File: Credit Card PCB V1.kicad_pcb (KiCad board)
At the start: 2 copper layers, 85.5 x 54 mm, 49 parts, among them J1 USB_C_Receptacle_USB2.0, SW1 RotaryEncoder, U1 USBLC6-2SC6, U2 ATmega32U2-A, Y1 16MHz

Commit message: Large Update
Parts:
- removed REF** (x4): MountingHole_2.2mm_M2_DIN965_Pad, MountingHole:MountingHole_2.2mm_M2_DIN965_Pad
- added C2: 1uF, Capacitor_SMD:C_0603_1608Metric, B.Cu at (159.8, 69.8)
- added C3: 10uF, Capacitor_SMD:C_0603_1608Metric, B.Cu at (159.8, 71.2)
- added F1: PTC 500mA, Fuse:Fuse_0603_1608Metric, B.Cu at (156.2, 73.8)
- added H0: MountingHole_Pad, MountingHole:MountingHole_2.2mm_M2_Pad_Via, F.Cu at (87.8, 68.5)
- added H1: MountingHole_Pad, MountingHole:MountingHole_2.2mm_M2_Pad_Via, F.Cu at (166.2, 68.5)
- added H2: MountingHole_Pad, MountingHole:MountingHole_2.2mm_M2_Pad_Via, F.Cu at (87.8, 115.5)
- added H3: MountingHole_Pad, MountingHole:MountingHole_2.2mm_M2_Pad_Via, F.Cu at (166.2, 115.5)
- added SW0: SW_Push, Button_Switch_SMD:SW_SPST_EVQP7C, B.Cu at (145.0, 66.5)
- moved R9 79.9 mm to (87.8, 86.8), turned to 90 degrees
- moved R7 79.1 mm to (87.8, 106.8), turned to 90 degrees
- moved R8 78.5 mm to (87.8, 96.8), turned to -90 degrees
- moved R4 17.2 mm to (157.2, 70.5), turned to 90 degrees
- moved U1 15.4 mm to (152.8, 74.0), turned to 135 degrees
- moved R3 14.5 mm to (156.5, 76.2), turned to -45 degrees
- moved R5 13.4 mm to (126.0, 75.0), turned to 90 degrees
- moved R2 13.2 mm to (155.0, 77.8), turned to -45 degrees
- moved R6 11.7 mm to (128.0, 75.0), turned to 90 degrees
- moved R1 8.00 mm to (167.0, 91.2), turned to 90 degrees
- moved C1 5.53 mm to (151.2, 78.2)
- moved C10 2.46 mm to (160.5, 74.2), turned to 135 degrees
- moved C8 1.60 mm to (159.2, 75.5), turned to 135 degrees
- moved C6 0.75 mm to (166.5, 76.8)
- moved C7 0.56 mm to (162.2, 72.5)
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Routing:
- net Net-(D12-A): track 104.4 -> 2.99 mm
- net /Indicator 2: track 21.6 -> 121.3 mm
- net Net-(D13-A): track 99.7 -> 2.99 mm
- net /Indicator 1: track 18.9 -> 113.1 mm
- net Net-(D14-A): track 95.0 -> 2.99 mm
- net /Indicator 0: track 16.2 -> 104.9 mm
- net Net-(U2-PC1/~{RESET}): track 0.00 -> 46.2 mm
- net /V Bus: track 0.00 -> 41.5 mm, vias 0 -> 4
- net /D+ Bus: track 0.00 -> 32.6 mm, vias 0 -> 2
- net /D- Bus: track 0.00 -> 31.9 mm, vias 0 -> 2
- net +5V: track 11.8 -> 41.4 mm
- net Net-(U2-D+): track 19.3 -> 6.10 mm, vias 2 -> 0
- net Net-(U2-~{HWB}/PD7): track 11.6 -> 2.77 mm
- net Net-(U2-D-): track 14.5 -> 6.19 mm
- net GND: track 11.4 -> 4.69 mm, vias 0 -> 3
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
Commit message: Chunky Update
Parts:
- moved C9 0.75 mm to (167.0, 79.5)
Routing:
- net +5V: track 41.4 -> 40.6 mm
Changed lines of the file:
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@@
   )
   (setup
+    (stackup
+      (layer "F.SilkS" (type "Top Silk Screen"))
+      (layer "F.Paste" (type "Top Solder Paste"))
+      (layer "F.Mask" (type "Top Solder Mask") (thickness 0.01))
+      (layer "F.Cu" (type "copper") (thickness 0.035))
+      (layer "dielectric 1" (type "core") (thickness 1.51) (material "FR4") (epsilon_r 4.5) (loss_tangent 0.02))
+      (layer "B.Cu" (type "copper") (thickness 0.035))
+      (layer "B.Mask" (type "Bottom Solder Mask") (thickness 0.01))
+      (layer "B.Paste" (type "Bottom Solder Paste"))
+      (layer "B.SilkS" (type "Bottom Silk Screen"))
+      (copper_finish "None")
+      (dielectric_constraints no)
+    )
     (pad_to_mask_clearance 0)
     (aux_axis_origin 84.25 119)
@@
   )
   (footprint "Capacitor_SMD:C_0603_1608Metric" (layer "B.Cu")
-    (at 167.75 79.5 90)
+    (at 167 79.5 90)
     (descr "Capacitor SMD 0603 (1608 Metric), square (rectangular) end terminal, IPC_7351 nominal, (Body size source: IPC-SM-782 page 76, https://www.pcb-3d.com/wordpress/wp-content/uploads/ipc-sm-782a_amendment_1_and_2.pdf), generated with kicad-footprint-generator")
     (tags "capacitor")
@@
   (segment (start 162.809835 82.231408) (end 164.952906 82.231408) (width 0.25) (layer "B.Cu") (net 7))
   (segment (start 164.952906 82.231408) (end 165.472361 81.711953) (width 0.25) (layer "B.Cu") (net 7))
-  (segment (start 167.75 80.275) (end 166.909314 80.275) (width 0.25) (layer "B.Cu") (net 7))
   (segment (start 160.5 76.75) (end 160.5 79.921573) (width 0.25) (layer "B.Cu") (net 7))
   (segment (start 166.909314 80.275) (end 165.472361 81.711953) (width 0.25) (layer "B.Cu") (net 7))

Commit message: Another Chunky Update
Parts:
- F1: footprint Fuse:Fuse_0603_1608Metric -> Fuse:Fuse_1206_3216Metric
- R5, R6: value R_Small -> 5.1k
- SW0: footprint Button_Switch_SMD:SW_SPST_EVQP7C -> Button_Switch_SMD:SW_SPST_SKQG_WithStem
- moved C10 23.2 mm to (167.0, 96.5), turned to -135 degrees
- moved R4 10.8 mm to (146.8, 68.0), turned to 180 degrees
- moved C9 9.44 mm to (161.3, 72.0), turned to 0 degrees
- moved SW0 6.73 mm to (139.2, 70.0)
- moved C2 5.47 mm to (161.3, 75.0)
- moved C8 5.15 mm to (164.2, 74.2), turned to -90 degrees
- moved C7 4.74 mm to (166.9, 73.4), turned to 180 degrees
- moved Y1 3.06 mm to (166.9, 76.4), turned to -90 degrees
- moved C3 2.72 mm to (161.3, 73.5)
- moved C6 2.68 mm to (166.9, 79.4), turned to 0 degrees
- moved F1 2.29 mm to (158.5, 73.5), turned to -90 degrees
- moved R5 0.25 mm to (125.8, 75.0)
- moved R6 0.25 mm to (128.2, 75.0)
- moved R1 0.25 mm to (166.8, 91.1)
- moved J1 0.22 mm to (127.0, 68.7)
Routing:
- net +5V: track 40.6 -> 56.6 mm
- net Net-(U2-PC1/~{RESET}): track 46.2 -> 37.5 mm
- net /V Bus: track 41.5 -> 44.0 mm
- net Net-(U2-PC0/XTAL2): track 5.90 -> 4.20 mm
- net Net-(U2-XTAL1): track 10.8 -> 9.70 mm
- net /D+ Bus: track 32.6 -> 31.6 mm
- added copper zone on B.Cu, net +5V

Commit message: STUFF
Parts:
- moved D7 0.50 mm to (111.2, 104.5)
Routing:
- net Net-(D7-A): track 3.49 -> 2.99 mm
- net /Row 2: track 73.5 -> 74.0 mm

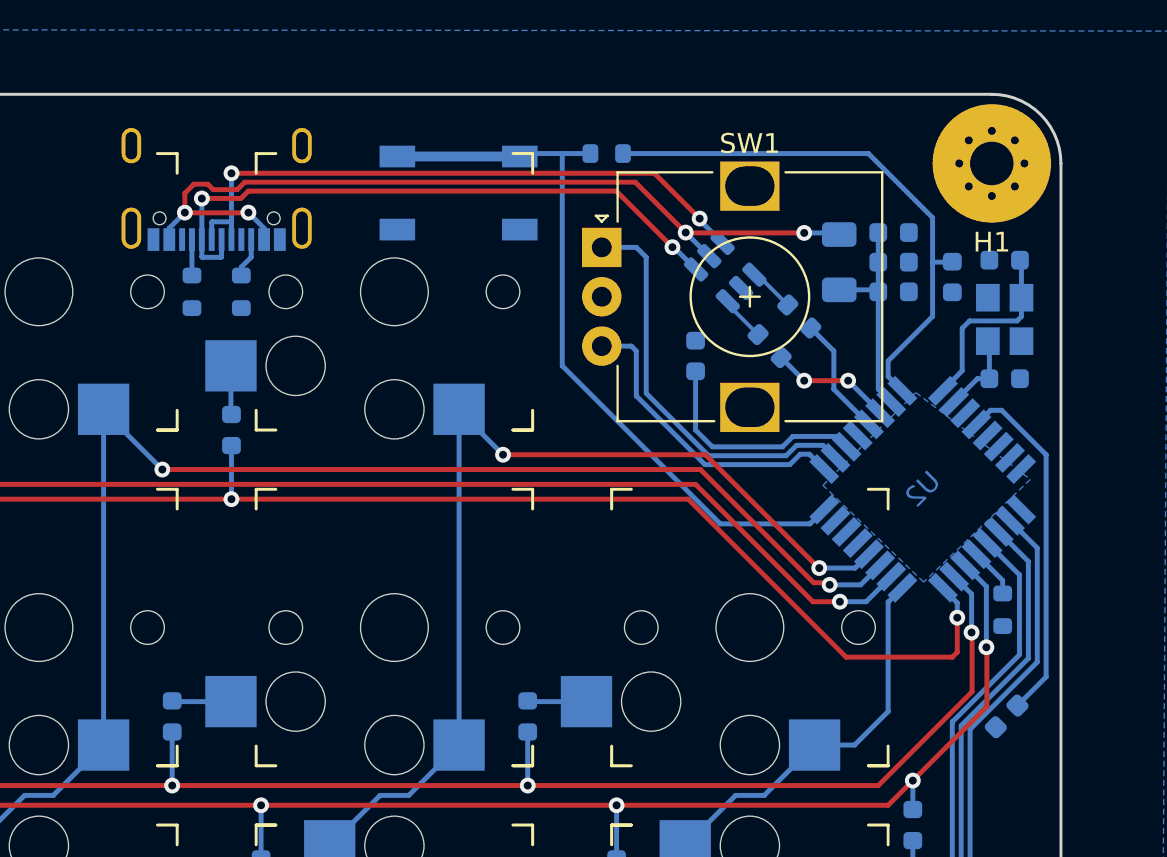
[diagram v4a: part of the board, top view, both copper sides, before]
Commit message: USB C Receptacle Change
Changed the usb c receptacle to a japanese standard one. I'm too lazy to go back and look up what it is.
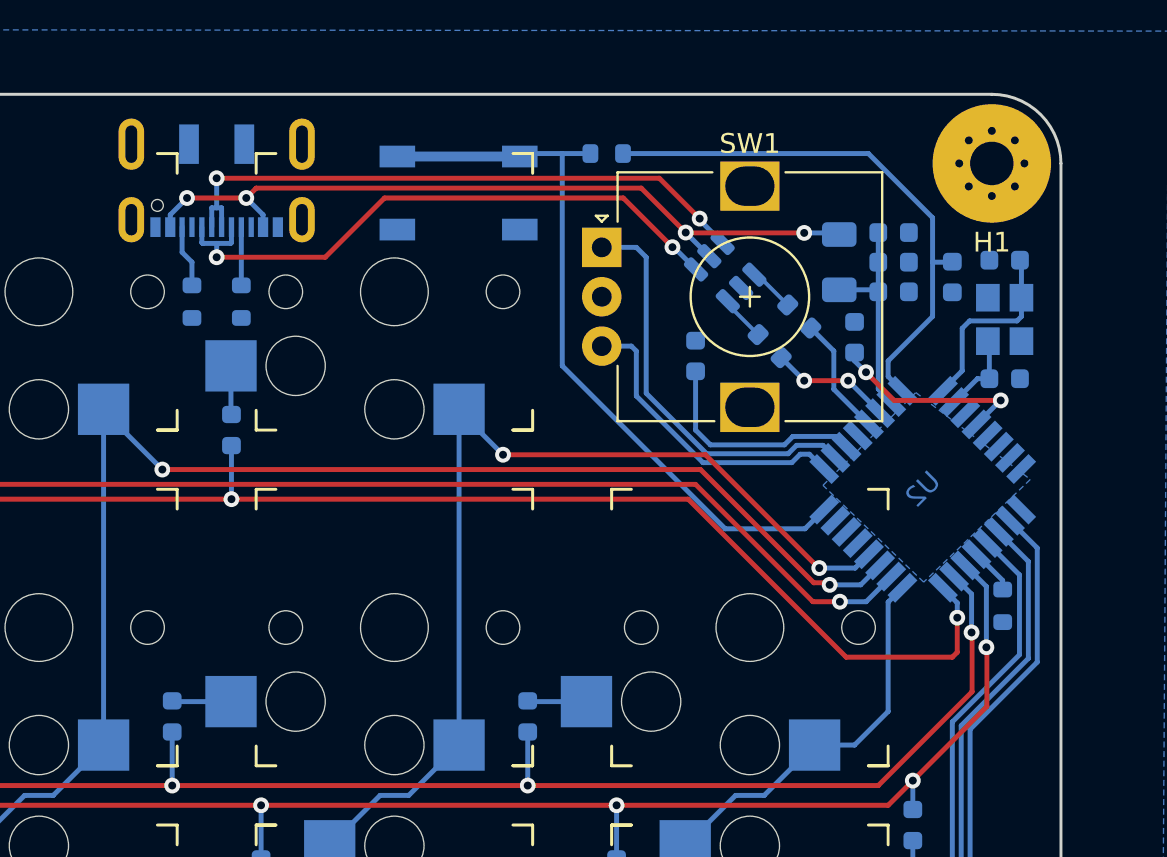
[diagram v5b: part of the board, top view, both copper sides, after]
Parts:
- J1: footprint Connector_USB:USB_C_Receptacle_GCT_USB4105-xx-A_16P_TopMnt_Horizontal -> Connector_USB:USB_C_Receptacle_JAE_DX07S016JA1R1500
- moved C10 20.7 mm to (159.3, 77.3), turned to 90 degrees
- moved R5 0.50 mm to (125.8, 75.5)
- moved R6 0.50 mm to (128.2, 75.5)
- moved R1 0.20 mm to (166.8, 90.9)
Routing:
- net +5V: track 56.6 -> 48.9 mm, vias 0 -> 2
- net /V Bus: track 44.0 -> 39.6 mm
- net Net-(J1-CC1): track 2.05 -> 3.16 mm
- net Net-(J1-CC2): track 2.03 -> 2.95 mm
- net /D- Bus: track 31.7 -> 30.8 mm
- net /D+ Bus: track 31.6 -> 31.0 mm

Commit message: Just a couple small things
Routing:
- net /Indicator 2: track 120.9 -> 121.8 mm
- net /Indicator 1: track 112.7 -> 113.6 mm
- net /Indicator 0: track 104.6 -> 105.4 mm
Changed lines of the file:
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@@
 (kicad_pcb (version 20221018) (generator pcbnew)
   (general
-    (thickness 1.6)
+    (thickness 1.16)
   )
   (paper "A4")
@@
       (layer "F.Mask" (type "Top Solder Mask") (thickness 0.01))
       (layer "F.Cu" (type "copper") (thickness 0.035))
-      (layer "dielectric 1" (type "core") (thickness 1.51) (material "FR4") (epsilon_r 4.5) (loss_tangent 0.02))
+      (layer "dielectric 1" (type "core") (thickness 1.07) (material "FR4") (epsilon_r 4.5) (loss_tangent 0.02))
       (layer "B.Cu" (type "copper") (thickness 0.035))
       (layer "B.Mask" (type "Bottom Solder Mask") (thickness 0.01))
@@
     (property "ki_keywords" "rotary switch encoder")
     (attr through_hole)
-    (fp_text reference "SW1" (at 0 -7.75) (layer "F.SilkS")
+    (fp_text reference "SW1" (at 0 -8) (layer "F.SilkS")
         (effects (font (size 1 1) (thickness 0.15)))
     )
@@
     (property "Sheetname" "")
     (attr smd)
-    (fp_text reference "MX2" (at -2.25 -2) (layer "B.SilkS")
+    (fp_text reference "MX2" (at -2.5 -2.25) (layer "B.SilkS")
         (effects (font (size 1 1) (thickness 0.15)) (justify mirror))
     )
@@
     (pad "S1" thru_hole oval locked (at 4.32 2.675) (size 1.3 2.3) (drill oval 0.6 1.6) (layers "*.Cu" "*.Mask")
       (net 1 "GND") (pinfunction "SHIELD") (pintype "passive"))
-    (model "${KICAD6_3DMODEL_DIR}/Connector_USB.3dshapes/USB_C_Receptacle_JAE_DX07S016JA1R1500.wrl"
+    (model "${KICAD6_3DMODEL_DIR}/Connector_USB.3dshapes/USB_C_Receptacle_JAE_DX07S016JA1R1500.wrl" hide
       (offset (xyz 0 0 0))
+      (scale (xyz 1 1 2.1))
+      (rotate (xyz 0 0 0))
+    )
+    (model "C:/Users/camer/Desktop/K3D-DX07S016JA1-V1_JAE_Proprietary.STEP"
+      (offset (xyz 0 1.1 1.58))
       (scale (xyz 1 1 1))
       (rotate (xyz 0 0 0))
@@
     (property "ki_keywords" "R resistor")
     (attr smd)
-    (fp_text reference "R5" (at -2.25 -0.5 90) (layer "B.SilkS")
+    (fp_text reference "R5" (at 2.25 -1.25 90) (layer "B.SilkS")
         (effects (font (size 1 1) (thickness 0.15)) (justify mirror))
     )
@@
     (property "ki_keywords" "switch normally-open pushbutton push-button")
     (attr smd)
-    (fp_text reference "SW0" (at 0 3.6) (layer "B.SilkS")
+    (fp_text reference "SW0" (at 0 -3.5 180) (layer "B.SilkS")
         (effects (font (size 1 1) (thickness 0.15)) (justify mirror))
     )
-    (fp_text value "SW_Push" (at 0 -3.6) (layer "B.Fab")
+    (fp_text value "SW_Push" (at 0 -3.6 180) (layer "B.Fab")
         (effects (font (size 1 1) (thickness 0.15)) (justify mirror))
     )
-    (fp_text user "KEEP-OUT ZONE" (at 2.5 0.2) (layer "Cmts.User")
+    (fp_text user "KEEP-OUT ZONE" (at 2.5 0.2 180) (layer "Cmts.User")
         (effects (font (size 0.2 0.2) (thickness 0.03)))
     )
-    (fp_text user "No F.Cu tracks" (at 2.5 -0.2) (layer "Cmts.User")
+    (fp_text user "No F.Cu tracks" (at 2.5 -0.2 180) (layer "Cmts.User")
         (effects (font (size 0.2 0.2) (thickness 0.03)))
     )
-    (fp_text user "No F.Cu tracks" (at -2.5 -0.2) (layer "Cmts.User")
+    (fp_text user "No F.Cu tracks" (at -2.5 -0.2 180) (layer "Cmts.User")
         (effects (font (size 0.2 0.2) (thickness 0.03)))
     )
-    (fp_text user "KEEP-OUT ZONE" (at -2.5 0.2) (layer "Cmts.User")
+    (fp_text user "KEEP-OUT ZONE" (at -2.5 0.2 180) (layer "Cmts.User")
         (effects (font (size 0.2 0.2) (thickness 0.03)))
     )
-    (fp_text user "${REFERENCE}" (at 0 0) (layer "B.Fab")
+    (fp_text user "${REFERENCE}" (at 0 0 180) (layer "B.Fab")
         (effects (font (size 0.4 0.4) (thickness 0.06)) (justify mirror))
     )
@@
       (rotate (xyz 0 0 0))
     )
+    (model "C:/Users/camer/Desktop/SKQGADE010/SKQGAD.STEP"
+      (offset (xyz 0 0 0))
+      (scale (xyz 1 1 1))
+      (rotate (xyz 0 0 0))
+    )
   )
   (footprint "Resistor_SMD:R_0603_1608Metric" (layer "B.Cu")
@@
     (property "ki_keywords" "R resistor")
     (attr smd)
-    (fp_text reference "R4" (at 2 0 90) (layer "B.SilkS")
+    (fp_text reference "R4" (at 0 1.25 180) (layer "B.SilkS")
         (effects (font (size 1 1) (thickness 0.15)) (justify mirror))
     )
@@
     (property "ki_keywords" "R resistor")
     (attr smd)
-    (fp_text reference "R6" (at -1.5 -1 90) (layer "B.SilkS")
+    (fp_text reference "R6" (at 2.25 1.5 90) (layer "B.SilkS")
         (effects (font (size 1 1) (thickness 0.15)) (justify mirror))
     )
@@
   (segment (start 156.548922 83.22387) (end 156.122792 83.65) (width 0.25) (layer "B.Cu") (net 10))
   (segment (start 87.75 107.575) (end 87.75 108.25) (width 0.25) (layer "B.Cu") (net 11))
-  (segment (start 165.15 107.236396) (end 165.15 97.15) (width 0.25) (layer "B.Cu") (net 11))
-  (segment (start 91.9 112.4) (end 159.986396 112.4) (width 0.25) (layer "B.Cu") (net 11))
-  (segment (start 159.986396 112.4) (end 165.15 107.236396) (width 0.25) (layer "B.Cu") (net 11))
+  (segment (start 87.75 108.25) (end 92.5 113) (width 0.25) (layer "B.Cu") (net 11))
+  (segment (start 160 113) (end 166 107) (width 0.25) (layer "B.Cu") (net 11))
+  (segment (start 92.5 113) (end 160 113) (width 0.25) (layer "B.Cu") (net 11))
   (segment (start 168.55 93.75) (end 168.55 87.971573) (width 0.25) (layer "B.Cu") (net 11))
-  (segment (start 165.15 97.15) (end 168.55 93.75) (width 0.25) (layer "B.Cu") (net 11))
-  (segment (start 87.75 108.25) (end 91.9 112.4) (width 0.25) (layer "B.Cu") (net 11))
+  (segment (start 166 96.3) (end 168.55 93.75) (width 0.25) (layer "B.Cu") (net 11))
   (segment (start 168.55 87.971573) (end 167.169417 86.59099) (width 0.25) (layer "B.Cu") (net 11))
-  (segment (start 89.25 109.113604) (end 92.086396 111.95) (width 0.25) (layer "B.Cu") (net 12))
-  (segment (start 89.25 99.075) (end 89.25 109.113604) (width 0.25) (layer "B.Cu") (net 12))
-  (segment (start 92.086396 111.95) (end 159.8 111.95) (width 0.25) (layer "B.Cu") (net 12))
+  (segment (start 166 107) (end 166 96.3) (width 0.25) (layer "B.Cu") (net 11))
+  (segment (start 165.55 106.813604) (end 165.55 96.113604) (width 0.25) (layer "B.Cu") (net 12))
+  (segment (start 159.813604 112.55) (end 165.55 106.813604) (width 0.25) (layer "B.Cu") (net 12))
   (segment (start 168.1 93.563604) (end 168.1 88.652944) (width 0.25) (layer "B.Cu") (net 12))
-  (segment (start 87.75 97.575) (end 89.25 99.075) (width 0.25) (layer "B.Cu") (net 12))
+  (segment (start 89.25 99.075) (end 89.25 109.113604) (width 0.25) (layer "B.Cu") (net 12))
+  (segment (start 92.686396 112.55) (end 159.813604 112.55) (width 0.25) (layer "B.Cu") (net 12))
+  (segment (start 165.55 96.113604) (end 168.1 93.563604) (width 0.25) (layer "B.Cu") (net 12))
   (segment (start 168.1 88.652944) (end 166.603732 87.156676) (width 0.25) (layer "B.Cu") (net 12))
-  (segment (start 164.7 96.963604) (end 168.1 93.563604) (width 0.25) (layer "B.Cu") (net 12))
-  (segment (start 164.7 107.05) (end 164.7 96.963604) (width 0.25) (layer "B.Cu") (net 12))
-  (segment (start 159.8 111.95) (end 164.7 107.05) (width 0.25) (layer "B.Cu") (net 12))
-  (segment (start 164.25 96.777208) (end 167.65 93.377208) (width 0.25) (layer "B.Cu") (net 13))
-  (segment (start 167.65 93.377208) (end 167.65 89.334314) (width 0.25) (layer "B.Cu") (net 13))
+  (segment (start 87.75 97.575) (end 89.25 99.075) (width 0.25) (layer "B.Cu") (net 12))
+  (segment (start 89.25 109.113604) (end 92.686396 112.55) (width 0.25) (layer "B.Cu") (net 12))
+  (segment (start 87.75 87.575) (end 89.7 89.525) (width 0.25) (layer "B.Cu") (net 13))
   (segment (start 167.65 89.334314) (end 166.038047 87.722361) (width 0.25) (layer "B.Cu") (net 13))
-  (segment (start 92.272792 111.5) (end 159.613604 111.5) (width 0.25) (layer "B.Cu") (net 13))
   (segment (start 89.7 89.525) (end 89.7 108.927208) (width 0.25) (layer "B.Cu") (net 13))
-  (segment (start 159.613604 111.5) (end 164.25 106.863604) (width 0.25) (layer "B.Cu") (net 13))
-  (segment (start 164.25 106.863604) (end 164.25 96.777208) (width 0.25) (layer "B.Cu") (net 13))
-  (segment (start 87.75 87.575) (end 89.7 89.525) (width 0.25) (layer "B.Cu") (net 13))
-  (segment (start 89.7 108.927208) (end 92.272792 111.5) (width 0.25) (layer "B.Cu") (net 13))
+  (segment (start 165.1 95.927208) (end 167.65 93.377208) (width 0.25) (layer "B.Cu") (net 13))
+  (segment (start 159.627208 112.1) (end 165.1 106.627208) (width 0.25) (layer "B.Cu") (net 13))
+  (segment (start 167.65 93.377208) (end 167.65 89.334314) (width 0.25) (layer "B.Cu") (net 13))
+  (segment (start 92.872792 112.1) (end 159.627208 112.1) (width 0.25) (layer "B.Cu") (net 13))
+  (segment (start 165.1 106.627208) (end 165.1 95.927208) (width 0.25) (layer "B.Cu") (net 13))
+  (segment (start 89.7 108.927208) (end 92.872792 112.1) (width 0.25) (layer "B.Cu") (net 13))
   (segment (start 166.8 89.615686) (end 166.8 90.075) (width 0.25) (layer "B.Cu") (net 14))
   (segment (start 165.472361 88.288047) (end 166.8 89.615686) (width 0.25) (layer "B.Cu") (net 14))
